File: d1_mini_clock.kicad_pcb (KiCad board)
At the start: 2 copper layers, 25.7 x 34.4 mm, 14 parts, among them J1 Conn_01x04, J2 Conn_01x03, P1 CONN_01X08, P2 CONN_01X08, U1 DS3231M, U2 74AHCT1G125

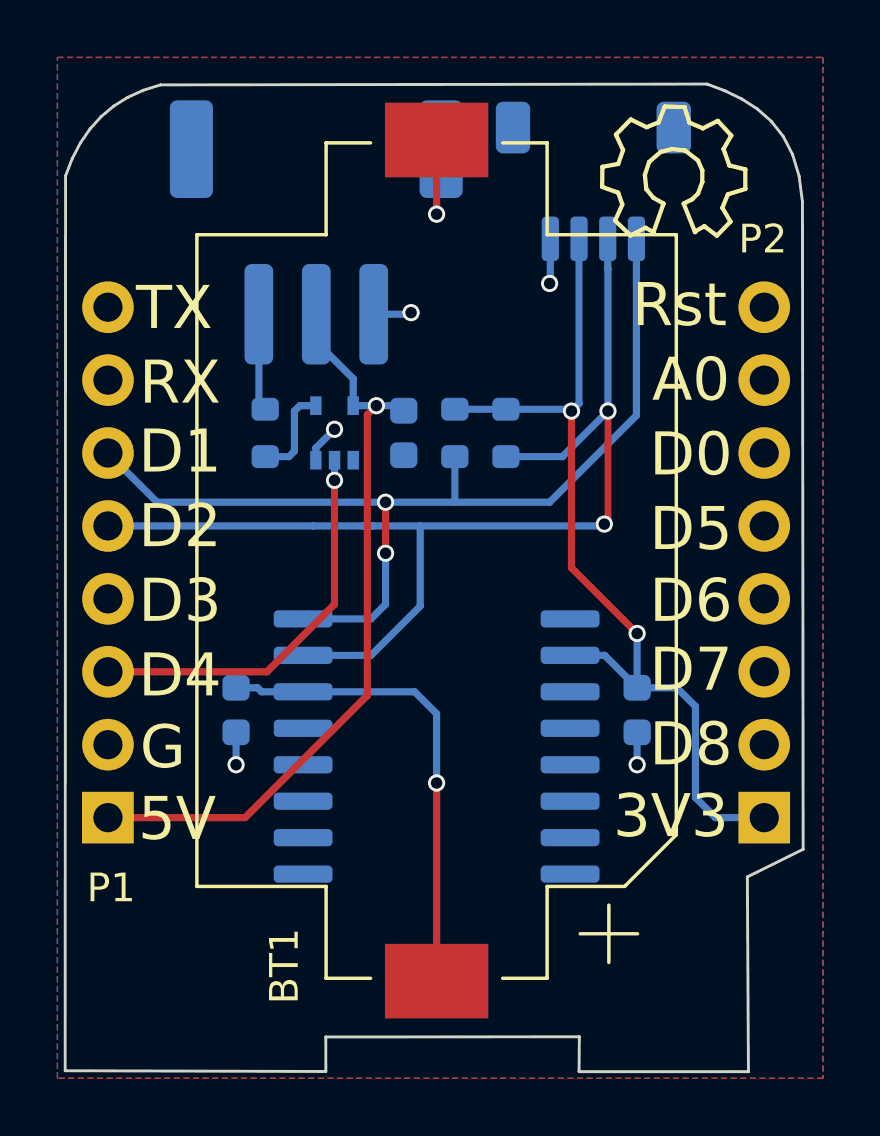
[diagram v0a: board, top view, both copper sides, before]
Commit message: Correcting inadequate trace width on 5V line.
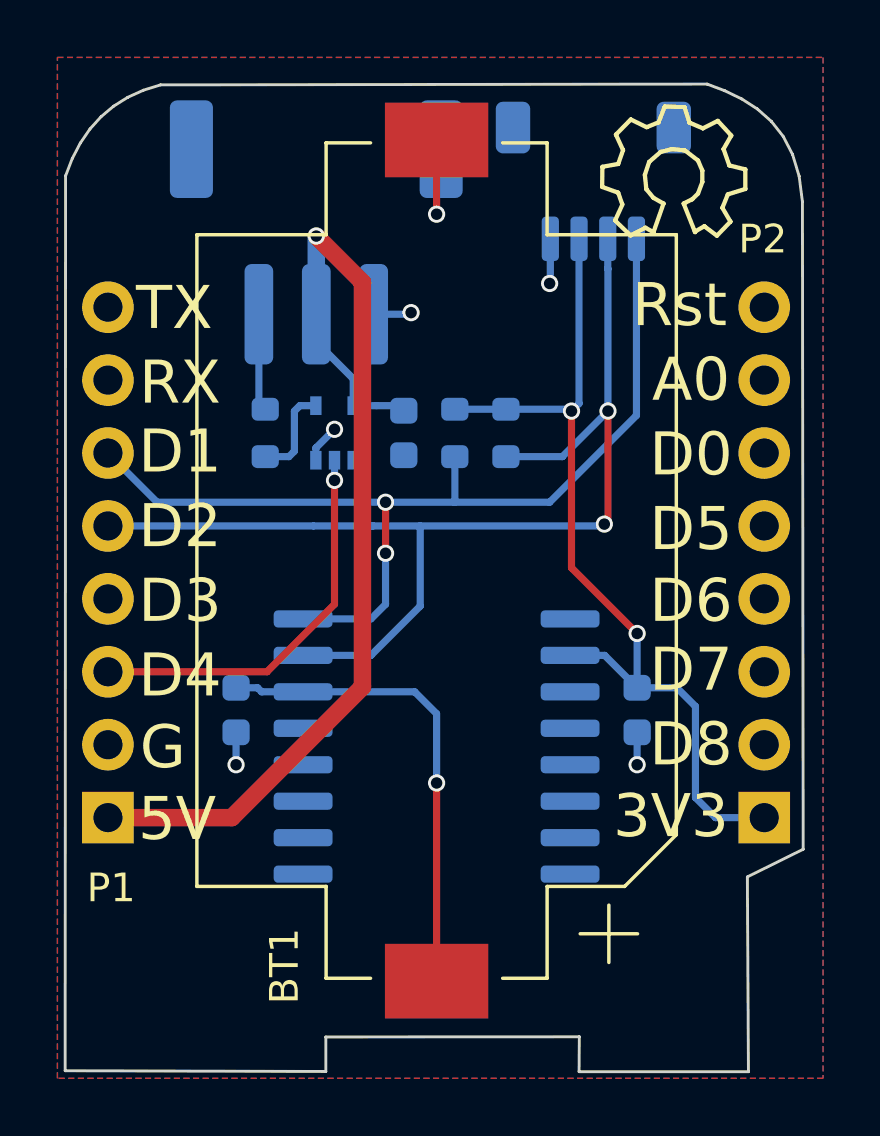
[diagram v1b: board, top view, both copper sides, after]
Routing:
- net VCC: track 26.6 -> 35.4 mm
